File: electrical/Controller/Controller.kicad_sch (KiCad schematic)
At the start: 48 parts, among them J1 USB4105-GF-A, J4 TC2030-NL, U1 USBLC6-2P6, U2 LP5912-3.3DRV, U3 W25Q16JVUXIQ, U4 RP2040, U5 ABPMRRV001PD2A3, Y1 12 MHz

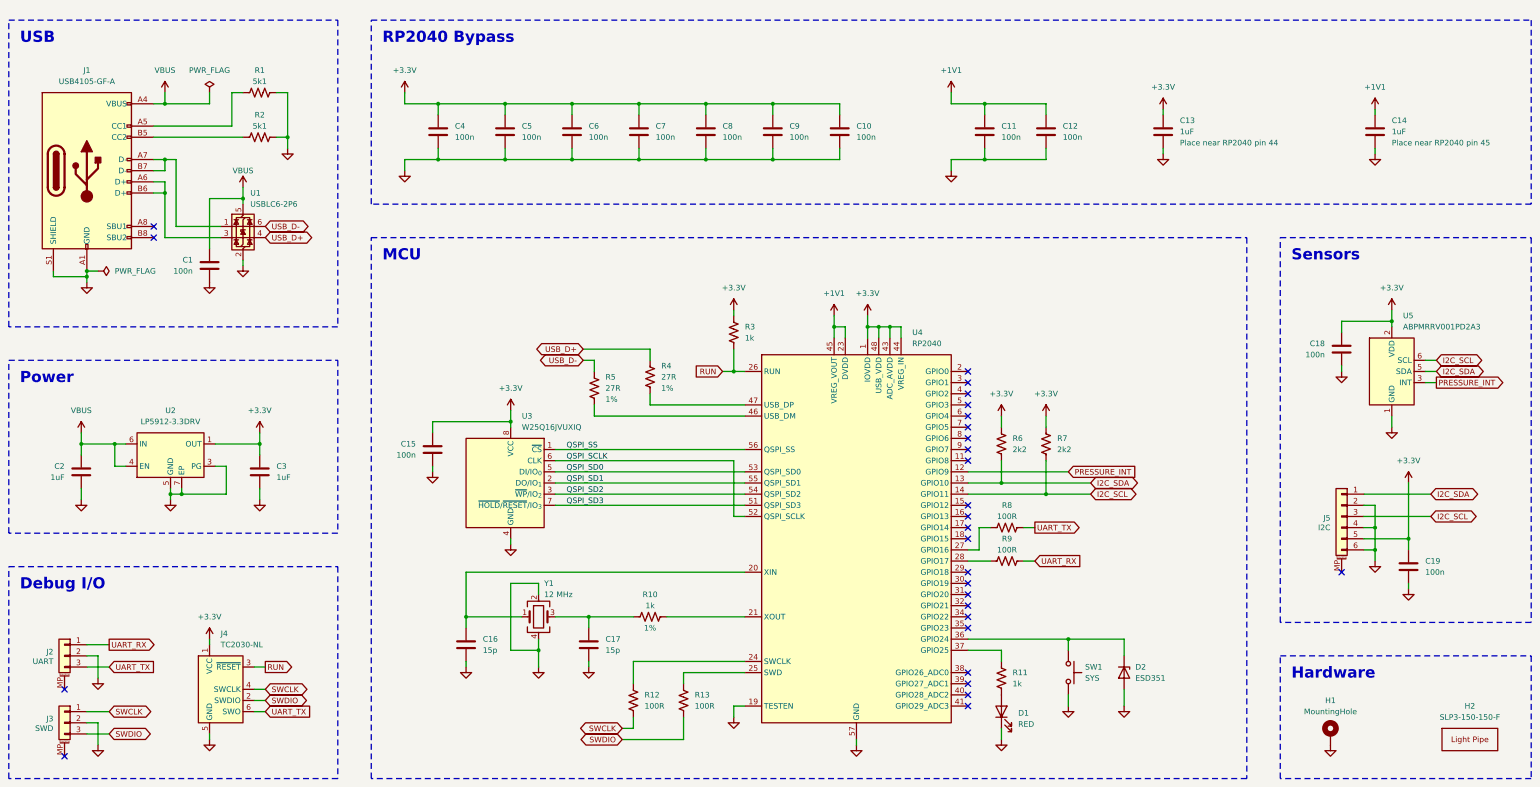
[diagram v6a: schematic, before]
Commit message: Redesign controller schematic with STM32
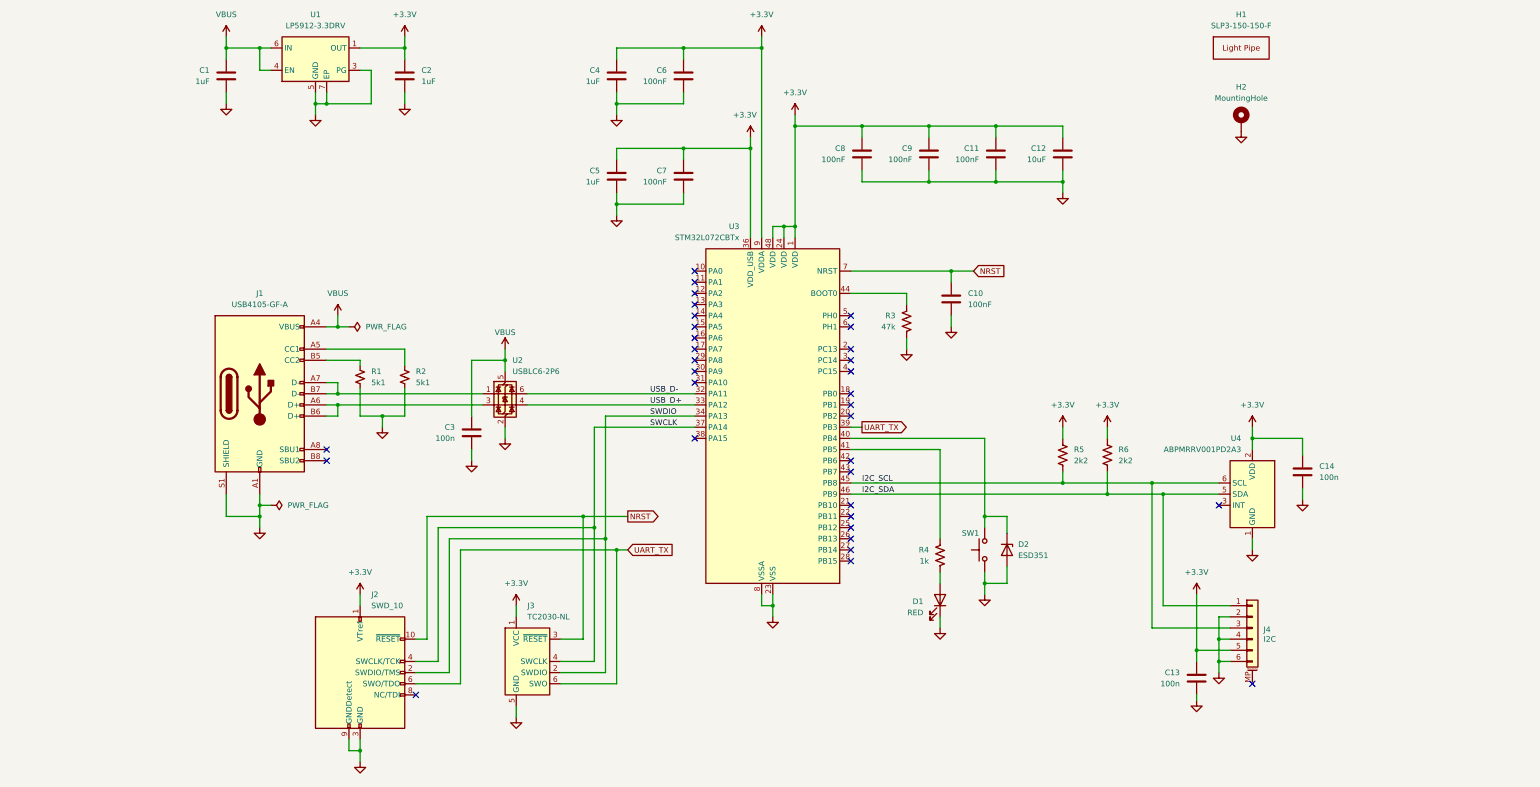
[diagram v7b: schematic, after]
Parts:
- removed C10, C15, C6: 100n, Capacitor_SMD:C_0402_1005Metric, symbol Device:C
- removed C13, C14: 1uF, Capacitor_SMD:C_0402_1005Metric, symbol Device:C
- removed C16, C17: 15p, Capacitor_SMD:C_0402_1005Metric, symbol Device:C
- removed J2, J3: ~, Connector_JST:JST_SH_SM03B-SRSS-TB_1x03-1MP_P1.00mm_Horizontal, symbol Connector_Generic_MountingPin:Conn_01x03_MountingPin
- removed R10: 1k, Resistor_SMD:R_0402_1005Metric, symbol Device:R_US
- removed R12, R13, R8, R9: 100R, Resistor_SMD:R_0402_1005Metric, symbol Device:R_US
- removed R4, R5: 27R, Resistor_SMD:R_0402_1005Metric, symbol Device:R_US
- removed U3: W25Q16JVUXIQ, Package_SON:Winbond_USON-8-1EP_3x2mm_P0.5mm_EP0.2x1.6mm, symbol Memory_Flash:W25Q16JVSS
- removed U4: RP2040, Package_DFN_QFN:QFN-56-1EP_7x7mm_P0.4mm_EP3.2x3.2mm, symbol MCU_RaspberryPi:RP2040
- removed Y1: 12 MHz, Crystal:Crystal_SMD_3225-4Pin_3.2x2.5mm, symbol Device:Crystal_GND24
- added C8, C9: 100nF, Capacitor_SMD:C_0402_1005Metric, symbol Device:C
- added J2: SWD_10, MidiConcertina:Samtech_FTSH-105-01-L-DH, symbol Connector:Conn_ARM_JTAG_SWD_10
- added U3: STM32L072CBTx, Package_QFP:LQFP-48_7x7mm_P0.5mm, symbol MCU_ST_STM32L0:STM32L072CBTx
- C10: renamed from C9; value 100n -> 100nF
- C11, C7: value 100n -> 100nF
- C12: value 100n -> 10uF; footprint Capacitor_SMD:C_0402_1005Metric -> Capacitor_SMD:C_0603_1608Metric; LCSC C1525 -> C96446; Part Samsung CL05B104KO5NNNC -> Samsung CL10A106MA8NRNC
- C4, C5: value 100n -> 1uF; LCSC C1525 -> C52923; Part Samsung CL05B104KO5NNNC -> Samsung CL05A105KA5NQNC
- C6: renamed from C8; value 100n -> 100nF
- R1: renamed from R2; symbol Device:R_US -> Device:R_Small_US
- R2: renamed from R1; symbol Device:R_US -> Device:R_Small_US
- R3: value 1k -> 47k; LCSC C11702 -> C25792; Part UNI-ROYAL 0402WGF1001TCE -> UNI-ROYAL 0402WGF4702TCE
- SW1: Label SYS -> (none)
- renumbered C2 to C1, C19 to C13, C18 to C14, C3 to C2, C1 to C3, H2 to H1, H1 to H2, J4 to J3, J5 to J4, R11 to R4, R6 to R5, R7 to R6, U2 to U1, U1 to U2, U5 to U4
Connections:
- net +1V1 is gone; now on net +3.3V: C11.1, C12.1
- net +3.3V: now also C8.1, C9.1, J2.1 (VTref), U3.1 (VDD), U3.24 (VDD), U3.36 (VDD_USB), U3.48 (VDD), U3.9 (VDDA); no longer C10.1, R3.1
- net GND: now also R3.2, C8.2, C9.2, J2.3 (GND), J2.5 (GND), J2.9 (GNDDetect), U3.23 (VSS), U3.35 (VSS), U3.47 (VSS), U3.8 (VSSA)
- net I2C_SCL: now also R5.2, U3.45 (PB8); no longer R6.2
- net I2C_SDA: now also R6.2, U3.46 (PB9); no longer R5.2
- net SWCLK: now also J2.4 (SWCLK/TCK), U3.37 (PA14)
- net SWDIO: now also J2.2 (SWDIO/TMS), U3.34 (PA13)
- net UART_TX: now also J2.6 (SWO/TDO), U3.39 (PB3)
- net USB_D+: now also U3.33 (PA12)
- net USB_D-: now also U3.32 (PA11)
- net at D2.1 (K), SW1.1: now also U3.40 (PB4)
- net at R4.1: now also U3.41 (PB5)
- net PRESSURE_INT: no longer names the net of U4.3 (INT)
- net RUN renamed NRST
- net NRST: now also C10.1, J2.10 (~{RESET}), U3.7 (NRST); no longer R3.2
- new net: R3.1, U3.44 (BOOT0)
- no-connect marks 28 -> 33
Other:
- note removed: "Debug I/O"
- note removed: "Hardware"
- note removed: "MCU"
- note removed: "Power"
- note removed: "RP2040 Bypass"
- note removed: "Sensors"
- note removed: "USB"
- moved on the sheet: C1, C10, C13, C14, C2, C3, C6, D1, D2, H1, H2, J1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

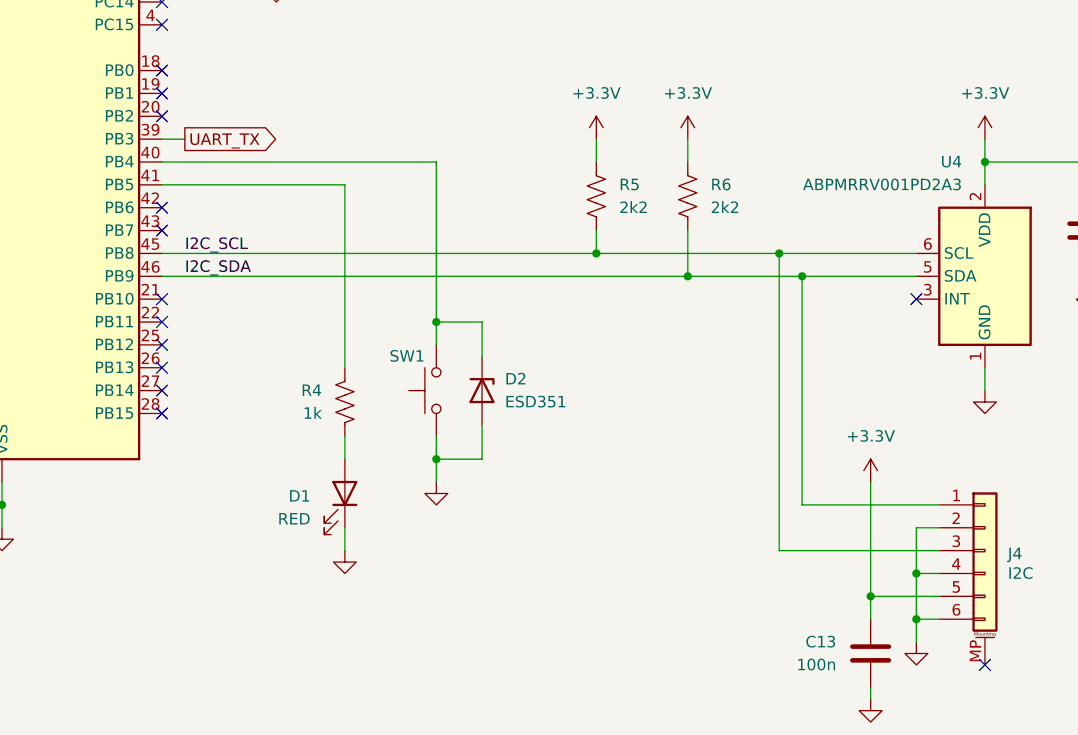
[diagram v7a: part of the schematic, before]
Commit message: Layout controller PCB with STM32 and updated connector pinout
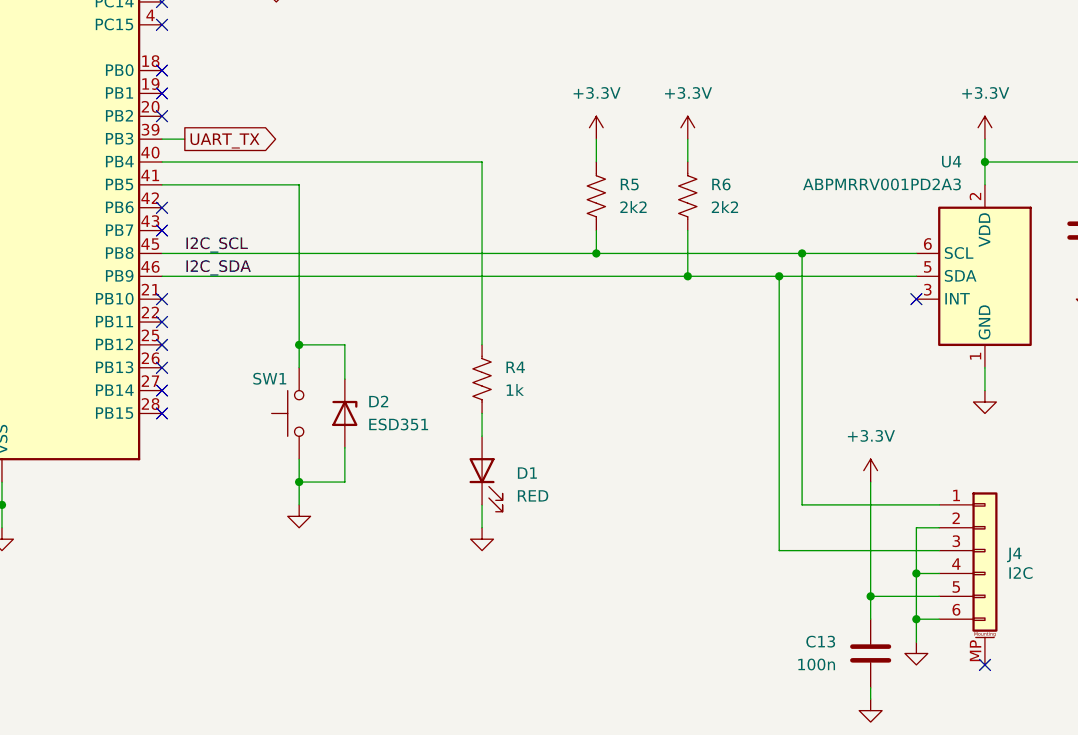
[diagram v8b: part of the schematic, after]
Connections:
- net I2C_SCL: now also J4.1 (Pin_1); no longer J4.3 (Pin_3)
- net I2C_SDA: now also J4.3 (Pin_3); no longer J4.1 (Pin_1)
- net at D2.1 (K), SW1.1: now also U3.41 (PB5); no longer U3.40 (PB4)
- net at R4.1: now also U3.40 (PB4); no longer U3.41 (PB5)
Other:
- moved on the sheet: D1, D2, R4, SW1
